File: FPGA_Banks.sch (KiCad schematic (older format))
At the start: 32 parts, among them U1 XA7Z020-1CLG400Q

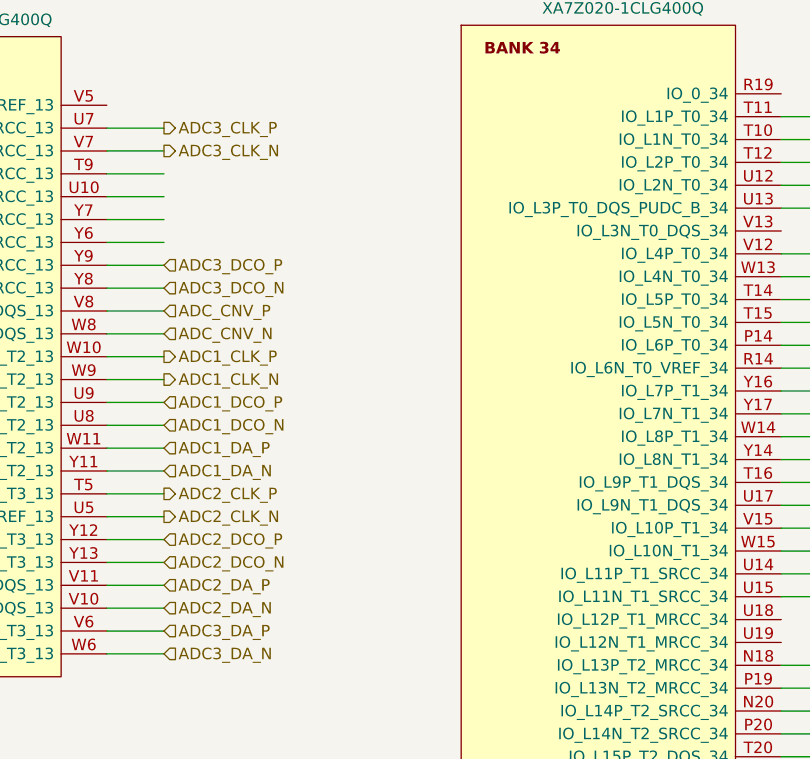
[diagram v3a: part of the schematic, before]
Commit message: Connections were made to FPGA banks
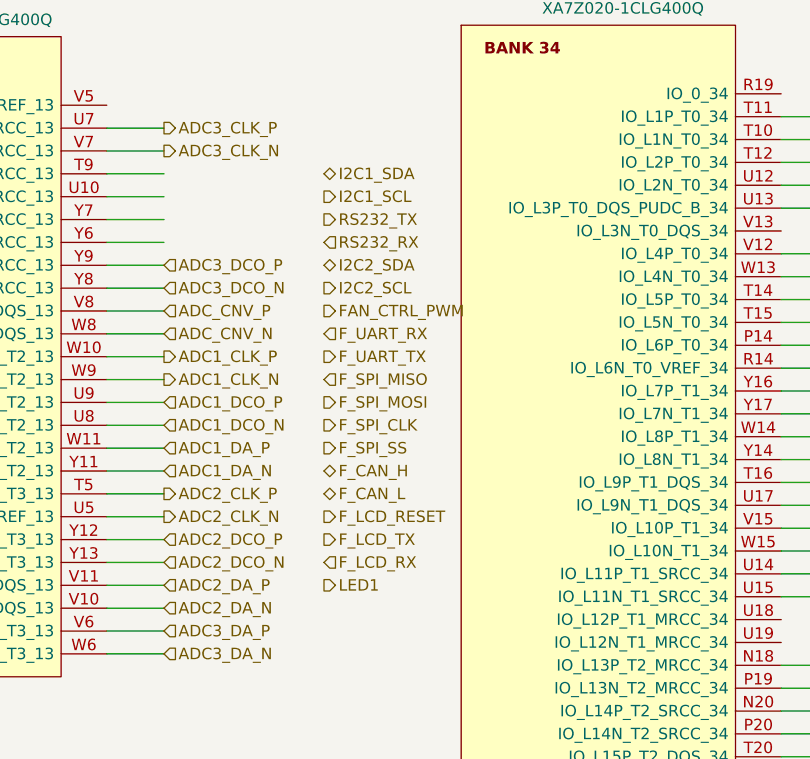
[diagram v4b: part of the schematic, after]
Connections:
- net labels added: FAN_CTRL_PWM, F_CAN_H, F_CAN_L, F_LCD_RESET, F_LCD_RX, F_LCD_TX, F_SPI_CLK, F_SPI_MISO, F_SPI_MOSI, F_SPI_SS, F_UART_RX, F_UART_TX, I2C1_SCL, I2C1_SDA, I2C2_SCL, I2C2_SDA, LED1, RS232_RX, RS232_TX
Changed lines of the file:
@@
 $Descr A3 16535 11693
 encoding utf-8
-Sheet 25 25
+Sheet 24 25
 Title ""
 Date ""
@@
 Wire Wire Line
 	2700 3850 2950 3850
+Text HLabel 3650 1750 2    50   BiDi ~ 0
+I2C1_SDA
+Text HLabel 3650 1850 2    50   Output ~ 0
+I2C1_SCL
+Text HLabel 3650 1950 2    50   Output ~ 0
+RS232_TX
+Text HLabel 3650 2050 2    50   Input ~ 0
+RS232_RX
+Text HLabel 3650 2150 2    50   BiDi ~ 0
+I2C2_SDA
+Text HLabel 3650 2250 2    50   Output ~ 0
+I2C2_SCL
+Text HLabel 3650 2350 2    50   Output ~ 0
+FAN_CTRL_PWM
+Text HLabel 3650 2450 2    50   Input ~ 0
+F_UART_RX
+Text HLabel 3650 2550 2    50   Output ~ 0
+F_UART_TX
+Text HLabel 3650 3050 2    50   BiDi ~ 0
+F_CAN_H
+Text HLabel 3650 3150 2    50   BiDi ~ 0
+F_CAN_L
+Text HLabel 3650 2650 2    50   Input ~ 0
+F_SPI_MISO
+Text HLabel 3650 2750 2    50   Output ~ 0
+F_SPI_MOSI
+Text HLabel 3650 2850 2    50   Output ~ 0
+F_SPI_CLK
+Text HLabel 3650 2950 2    50   Output ~ 0
+F_SPI_SS
+Text HLabel 3650 3250 2    50   Output ~ 0
+F_LCD_RESET
+Text HLabel 3650 3350 2    50   Output ~ 0
+F_LCD_TX
+Text HLabel 3650 3450 2    50   Input ~ 0
+F_LCD_RX
+Text HLabel 3650 3550 2    50   Output ~ 0
+LED1
 Wire Bus Line
 	11200 3350 11200 3600

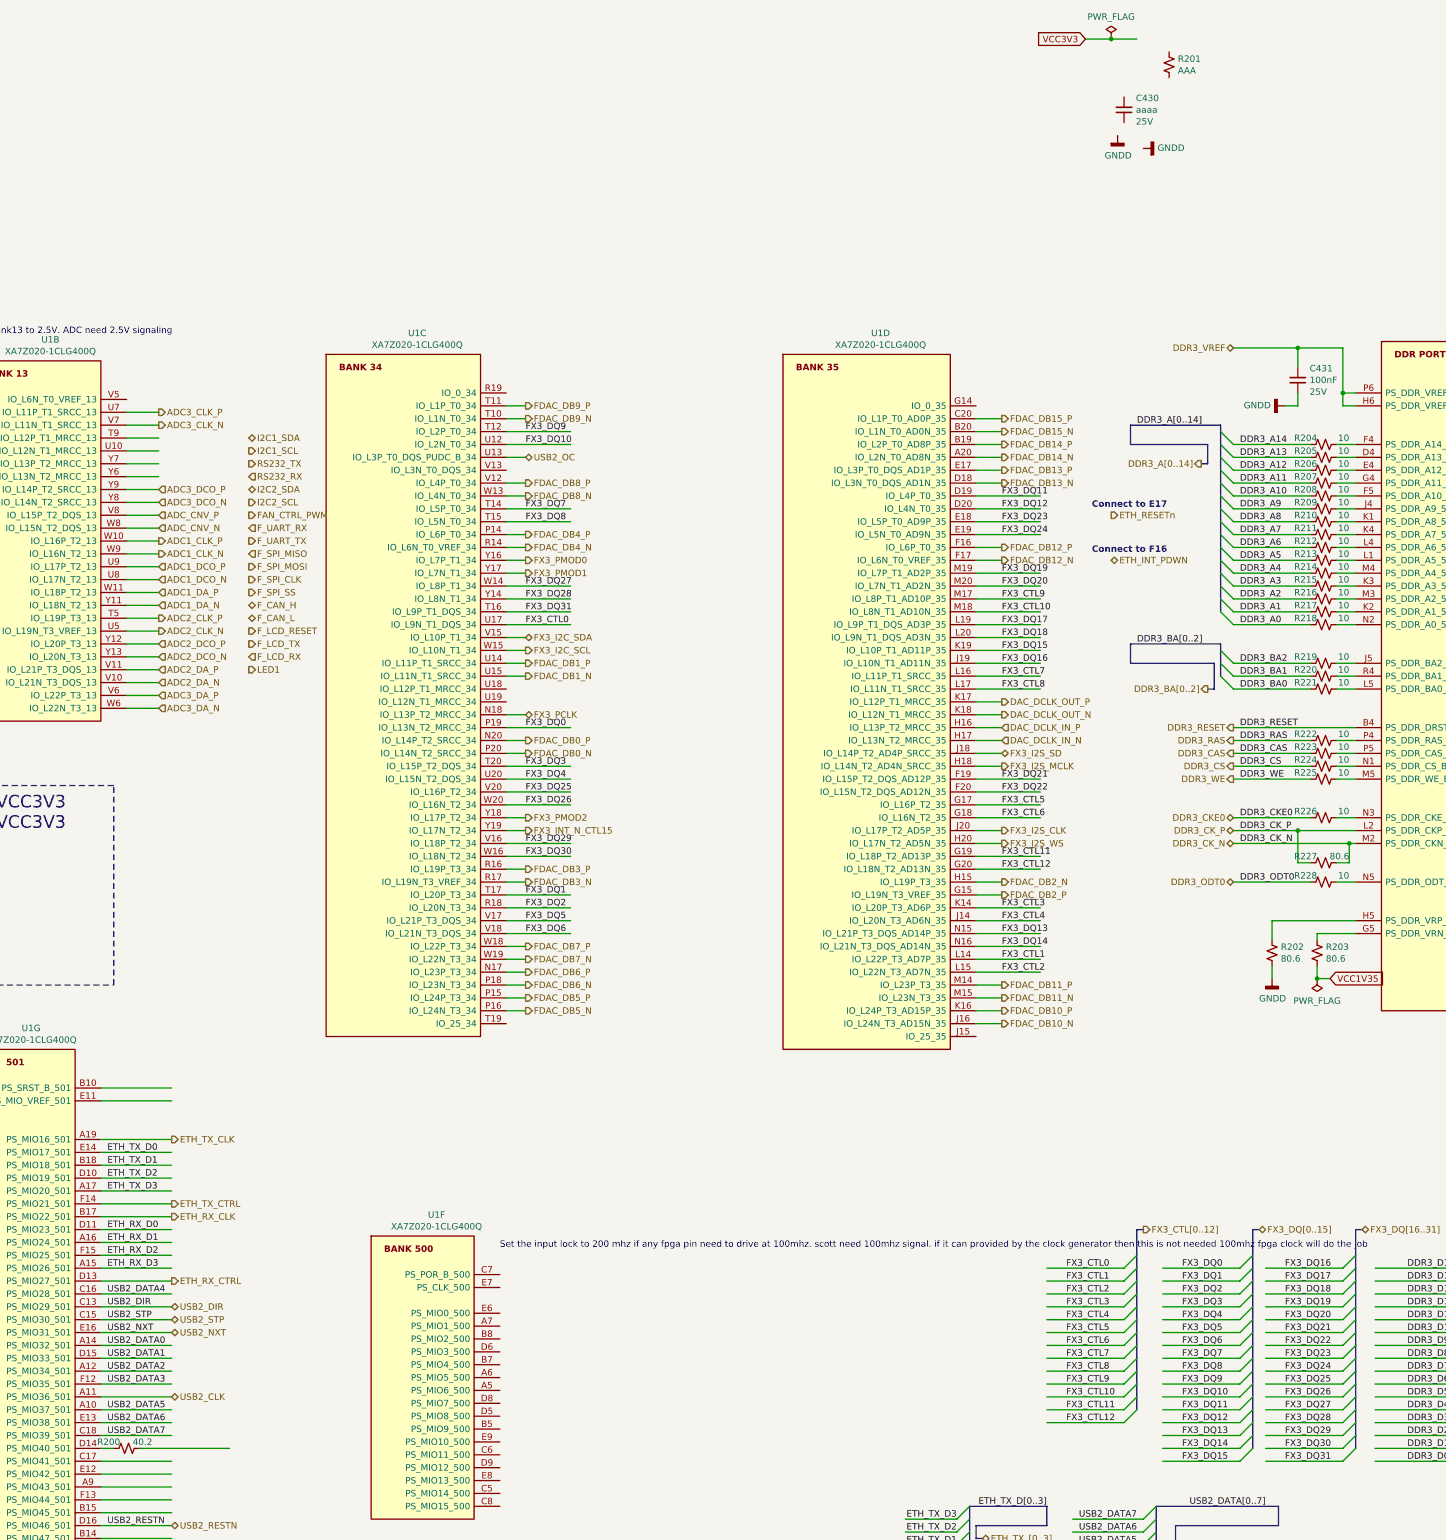
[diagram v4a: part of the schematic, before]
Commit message: Corrected PCB import errors
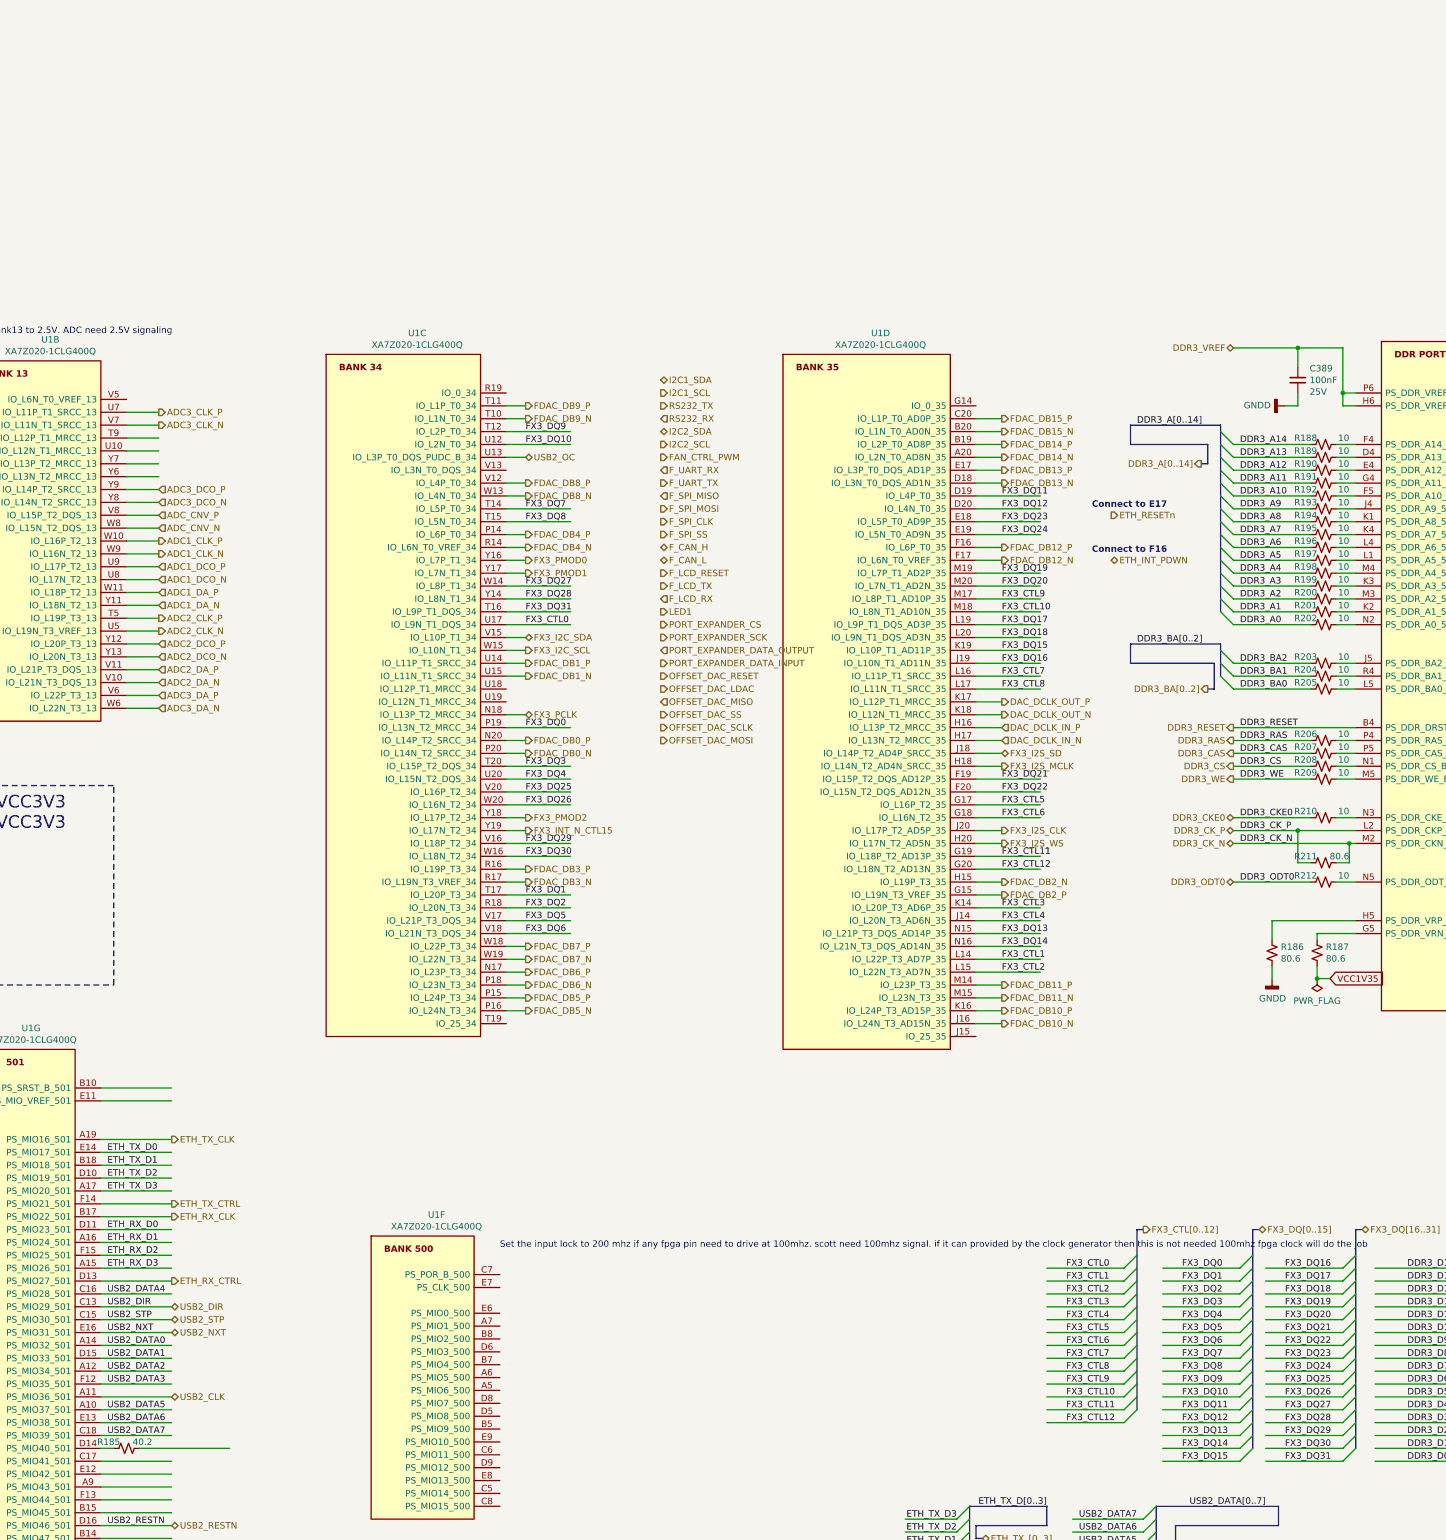
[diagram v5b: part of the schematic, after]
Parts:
- removed C430: aaaa, Capacitor_SMD:C_0603_1608Metric_Pad1.08x0.95mm_HandSolder, symbol Device:C_Small
- removed R201: AAA, Resistor_SMD:R_0603_1608Metric_Pad0.98x0.95mm_HandSolder, symbol Device:R_Small_US
- renumbered C431 to C389, R200 to R185, R202 to R186, R203 to R187, R204 to R188, R205 to R189, R206 to R190, R207 to R191, R208 to R192, R209 to R193, R210 to R194, R211 to R195, R212 to R196, R213 to R197, R214 to R198, R215 to R199, R216 to R200, R217 to R201, R218 to R202, R219 to R203, R220 to R204, R221 to R205, R222 to R206, R223 to R207, R224 to R208, R225 to R209, R226 to R210, R227 to R211, R228 to R212
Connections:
- net labels added: OFFSET_DAC_LDAC, OFFSET_DAC_MISO, OFFSET_DAC_MOSI, OFFSET_DAC_RESET, OFFSET_DAC_SCLK, OFFSET_DAC_SS, PORT_EXPANDER_CS, PORT_EXPANDER_DATA_INPUT, PORT_EXPANDER_DATA_OUTPUT, PORT_EXPANDER_SCK
- net labels removed: VCC3V3
- wire segments 370 -> 368
